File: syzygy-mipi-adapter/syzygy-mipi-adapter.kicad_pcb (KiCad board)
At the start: 4 copper layers, 45 x 70 mm, 94 parts, among them J1 Conn_02x06_Odd_Even, J2 SYZYGY_STD, J3 USB_C_Receptacle_USB2.0_16P, J4 SM03B-SRSS-TB, J6 501951-2230, J7 501951-2230, J8 501951-2230, Q1 DMG1024UV-7, Q2 DMG1024UV-7, U1 RP2350_80QFN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

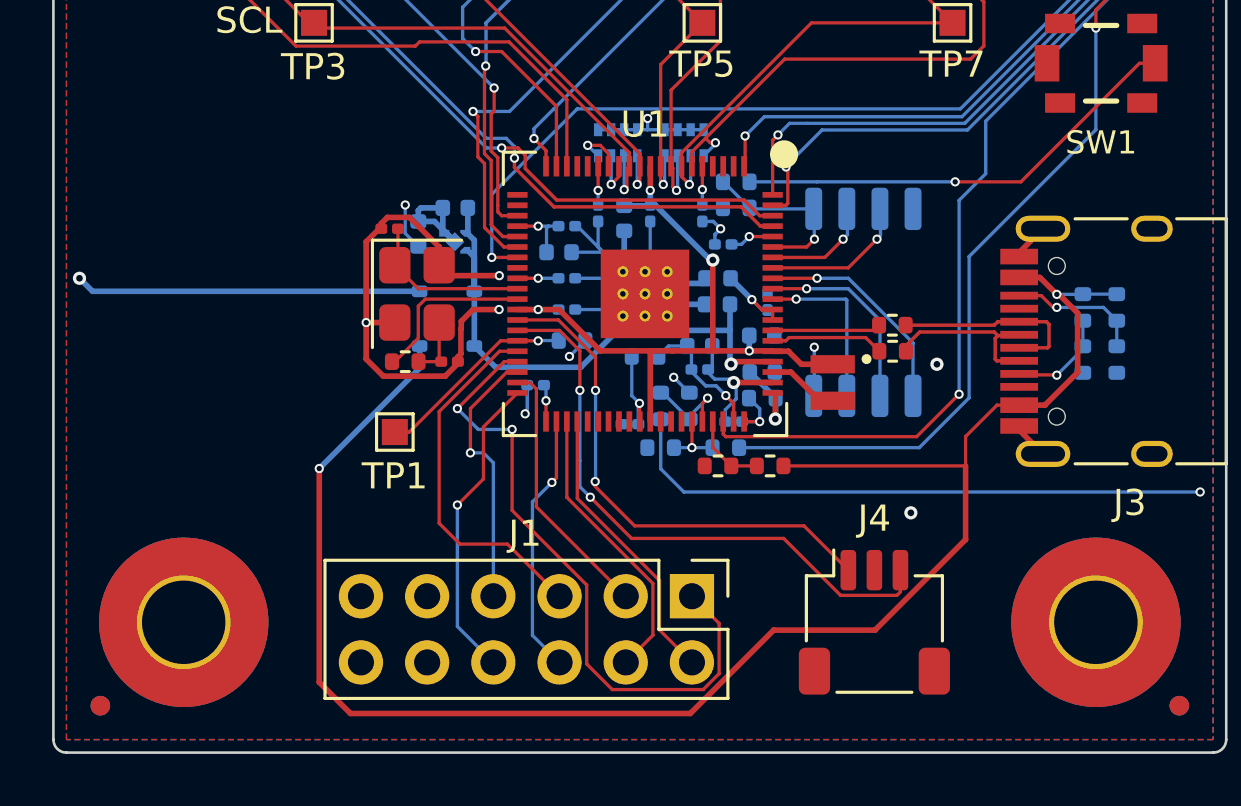
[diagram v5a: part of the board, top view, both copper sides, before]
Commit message: Sort out decoupling caps
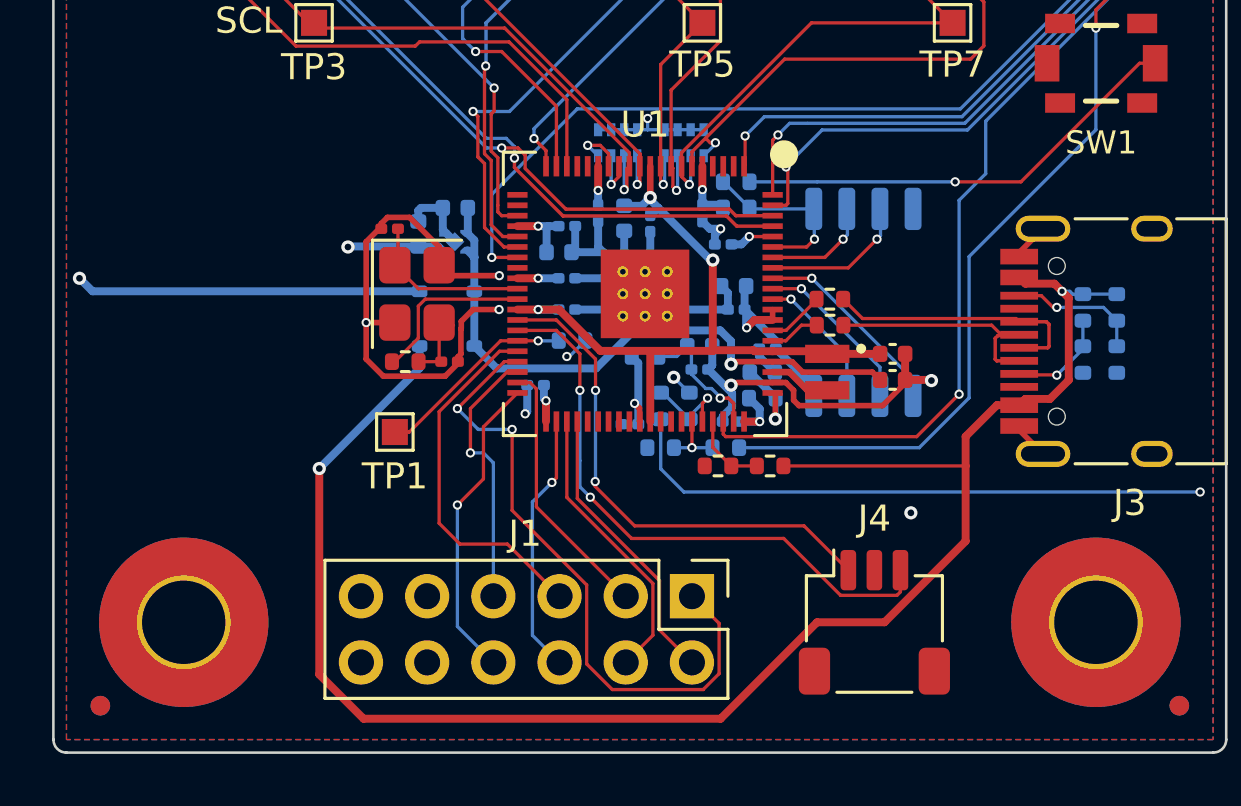
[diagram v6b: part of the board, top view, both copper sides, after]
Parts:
- added C13: 0.1u, Capacitor_SMD:C_0201_0603Metric, B.Cu at (126.0, 117.3)
- C1, C2: moved to F.Cu
- moved C1 7.32 mm to (132.2, 115.7), turned to 0 degrees
- moved C2 5.07 mm to (132.2, 114.7)
- moved C10 4.30 mm to (126.2, 113.0)
- moved R5 2.60 mm to (129.8, 112.6)
- moved R6 2.60 mm to (129.8, 113.6)
- moved C43 1.80 mm to (127.4, 114.5), turned to 180 degrees
- moved C9 0.67 mm to (126.1, 112.1)
- moved L1 0.45 mm to (129.7, 115.4)
- moved C6 0.40 mm to (122.9, 109.7)
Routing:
- net GND: track 148.2 -> 153.6 mm
- net P3V3D: track 38.2 -> 42.8 mm, vias 18 -> 17
- net /USB_D-: track 7.31 -> 10.2 mm
- net /USB_D+: track 7.61 -> 10.3 mm
- net Net-(U1-USB_DM): track 4.36 -> 1.94 mm
- net Net-(D1-K): track 21.8 -> 23.9 mm
- net Net-(U1-USB_DP): track 4.17 -> 2.20 mm
- net P1V1D: track 26.2 -> 27.9 mm, vias 4 -> 3
- net /RP_QSPI.SD3: track 6.53 -> 5.30 mm
- net /RP_QSPI.SCLK: track 7.52 -> 6.46 mm
- net /RP_QSPI.SD0: track 8.44 -> 7.62 mm

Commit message: Separate 3.3V rails for MSU vs Syzygy
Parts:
- added F1: MF-FSMF035X-2, Resistor_SMD:R_0603_1608Metric, B.Cu at (116.0, 109.7)
- moved C12 1.50 mm to (112.5, 110.1)
- moved U11 1.24 mm to (114.2, 110.4)
- moved C11 1.24 mm to (114.2, 109.1)
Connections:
- C10 pad 1: P3V3D -> PMCUD
- C11 pad 1: Net-(D1-K) -> Net-(U11-EN)
- C12 pad 1: P3V3D -> PMCUD
- C13 pad 1: P3V3D -> PMCUD
- C33 pad 1: P3V3D -> PMCUD
- C34 pad 1: P3V3D -> PMCUD
- C36 pad 1: P3V3D -> PMCUD
- C37 pad 1: P3V3D -> PMCUD
- C39 pad 1: P3V3D -> PMCUD
- C40 pad 1: P3V3D -> PMCUD
- C41 pad 1: P3V3D -> PMCUD
- C42 pad 1: P3V3D -> PMCUD
- C43 pad 1: P3V3D -> PMCUD
- C9 pad 1: P3V3D -> PMCUD
- J2 pad 40: /SZG_3V3 -> P3V3D
- R1 pad 2: P3V3D -> PMCUD
- R10 pad 1: /SZG_3V3 -> P3V3D
- R18 pad 2: /SZG_3V3 -> P3V3D
- R2 pad 2: P3V3D -> PMCUD
- R4 pad 1: P3V3D -> PMCUD
- R9 pad 2: P3V3D -> PMCUD
- U1 pad 15: P3V3D -> PMCUD
- U1 pad 24: P3V3D -> PMCUD
- U1 pad 29: P3V3D -> PMCUD
- U1 pad 41: P3V3D -> PMCUD
- U1 pad 5: P3V3D -> PMCUD
- U1 pad 50: P3V3D -> PMCUD
- U1 pad 60: P3V3D -> PMCUD
- U1 pad 68: P3V3D -> PMCUD
- U1 pad 69: P3V3D -> PMCUD
- U1 pad 76: P3V3D -> PMCUD
- U11 pad 1: P3V3D -> PMCUD
- U11 pad 3: Net-(D1-K) -> Net-(U11-EN)
- U11 pad 4: Net-(D1-K) -> Net-(U11-EN)
- U2 pad 8: P3V3D -> PMCUD
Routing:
- net /SZG_3V3: track 74.6 -> 0.00 mm, vias 3 -> 0
- net PMCUD: track 0.00 -> 28.8 mm, vias 0 -> 11
- net P3V3D: track 42.8 -> 16.1 mm, vias 17 -> 11
- net Net-(U11-EN): track 0.00 -> 3.14 mm
- net GND: track 153.6 -> 156.0 mm, vias 80 -> 81
- net Net-(D1-K): track 23.9 -> 22.0 mm
- added copper zone on In2.Cu, net PMCUD
